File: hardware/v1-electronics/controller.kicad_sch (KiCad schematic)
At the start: 35 parts, among them IC1 IS31FL3733-QFLS4-TR, IC2 IS31FL3733-QFLS4-TR, J2 Conn_01x03, U1 MDBT50Q-1MV2

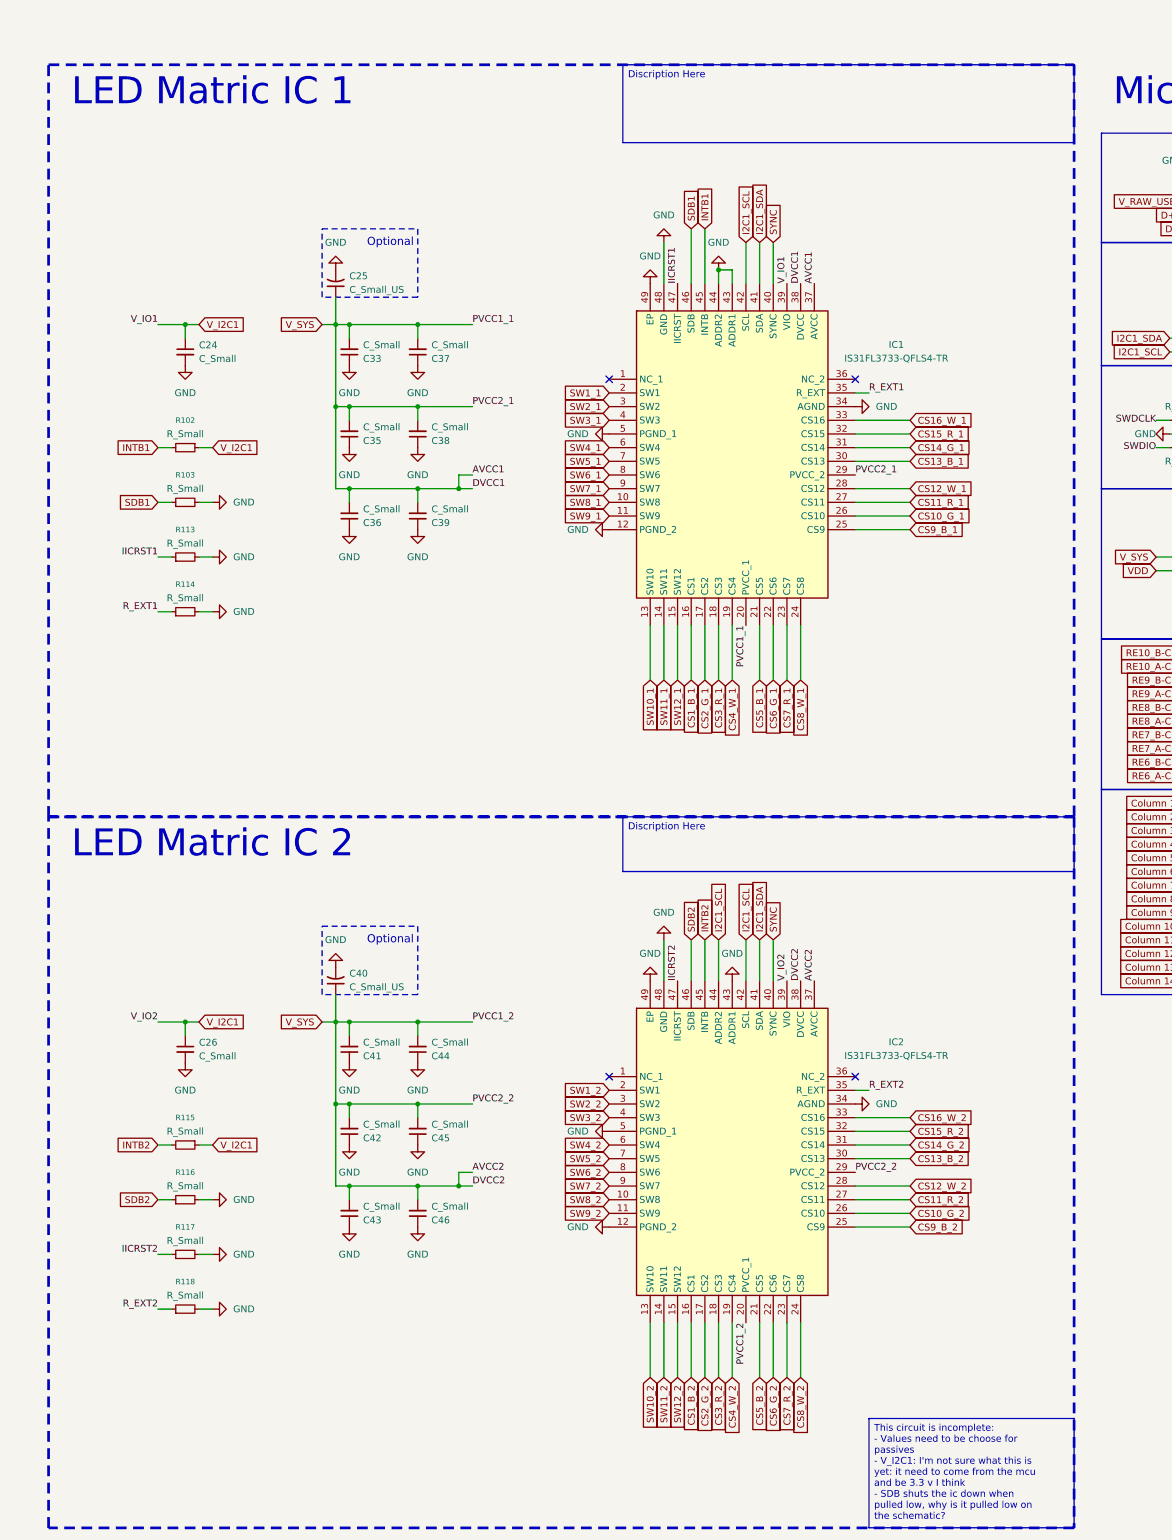
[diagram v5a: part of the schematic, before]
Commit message: refactor(v1 hardware): power train
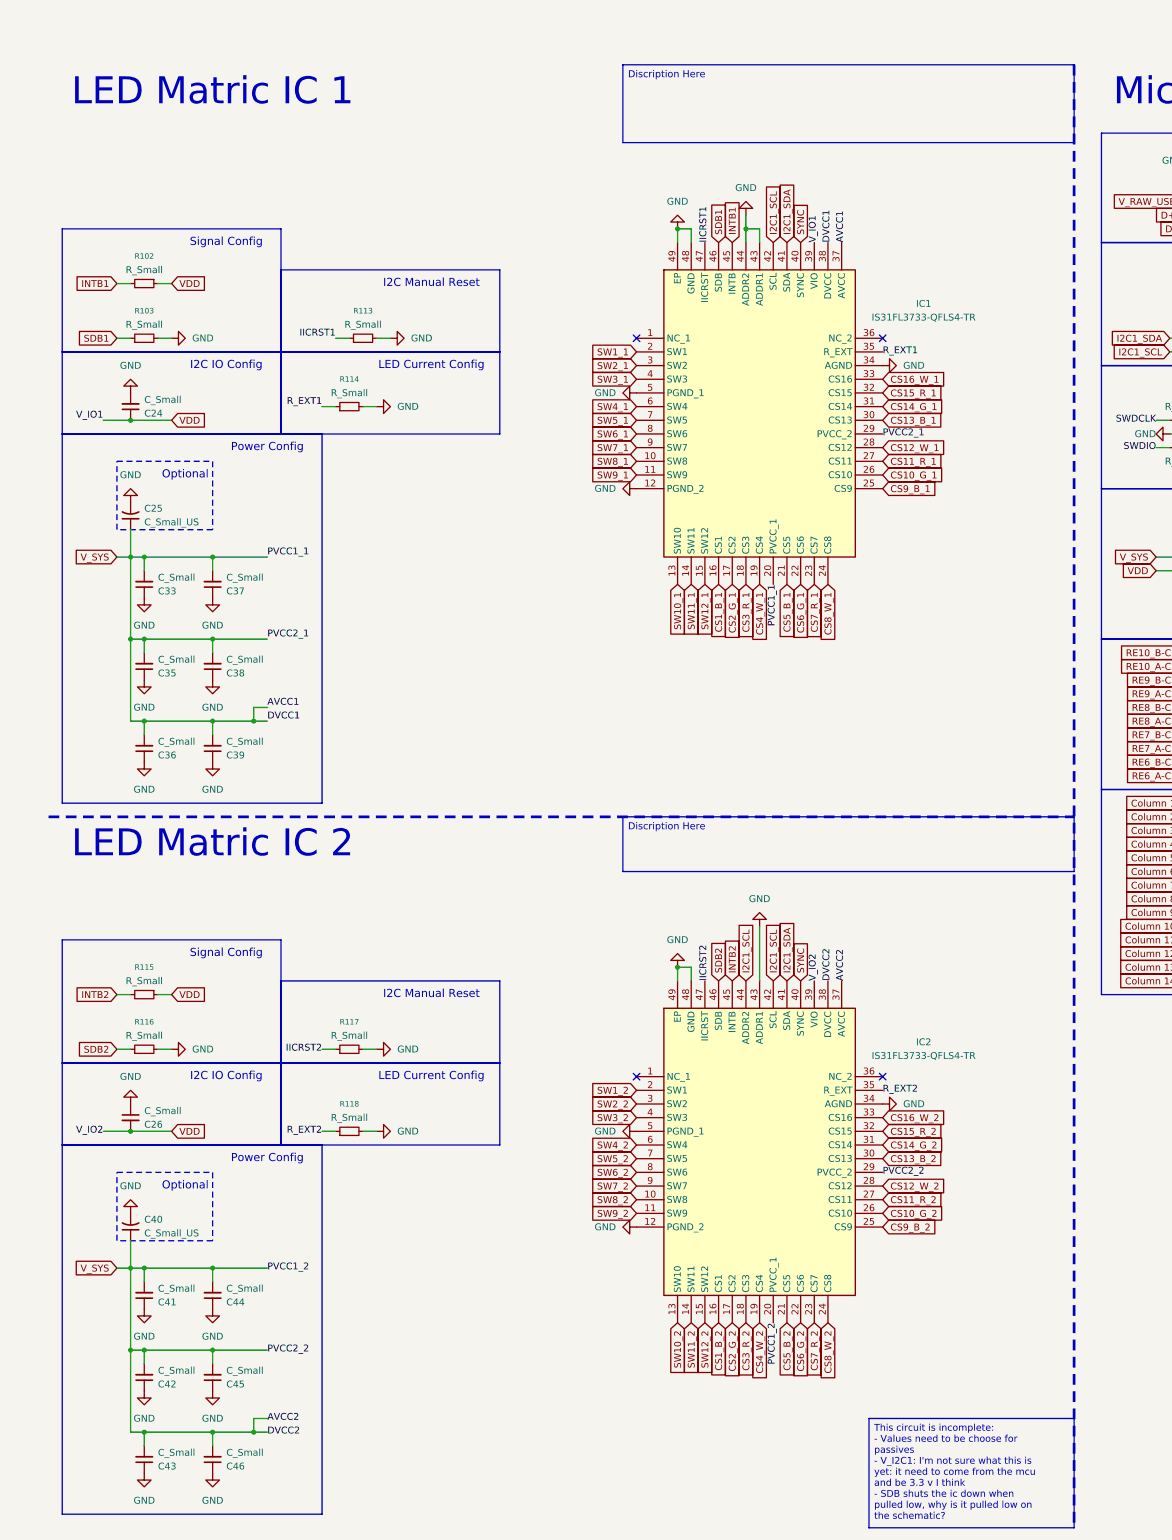
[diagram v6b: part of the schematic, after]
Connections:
- net GND: now also C26.1; no longer C26.2
- net VDD: now also C24.1, C26.2, IC1.39 (VIO), IC2.39 (VIO), R102.1, R115.1
- removed net V_I2C1: C24.1, C26.1, IC1.39 (VIO), IC2.39 (VIO), R102.1, R115.1
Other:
- note added: "I2C IO Config"
- note added: "I2C Manual Reset"
- note added: "LED Current Config"
- note added: "Signal Config"
- moved on the sheet: C24, C25, C26, C33, C35, C36, C37, C38, C39, C40, C41, C42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

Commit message: refactor(v1 hardware): add different charger ic & clean-up schematics
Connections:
- net INTB1 renamed IS31FL3733_INTB1
- net INTB2 renamed IS31FL3733_INTB2
- net SDB1 renamed IS31FL3733_SDB1
- net SDB2 renamed IS31FL3733_SDB2
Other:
- note added: "Set up resets for the device. Centralize the decoupling for V_SYS"
- note removed: "I'll likily need to change to use a I2C charger."
- note removed: "Set up resets for the device."
- moved on the sheet: IC1, IC2, R102, R103, R113, R115, R116, R117
